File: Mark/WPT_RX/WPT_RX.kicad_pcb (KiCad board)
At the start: 2 copper layers, 53 parts, among them J1 Conn_01x01, J2 Conn_01x01, J3 SMA, J4 SMA, J5 SMA, J6 Conn_01x01, J7 Conn_01x01, J8 From PI Board, Q1 NMOS, U1 LMC6032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

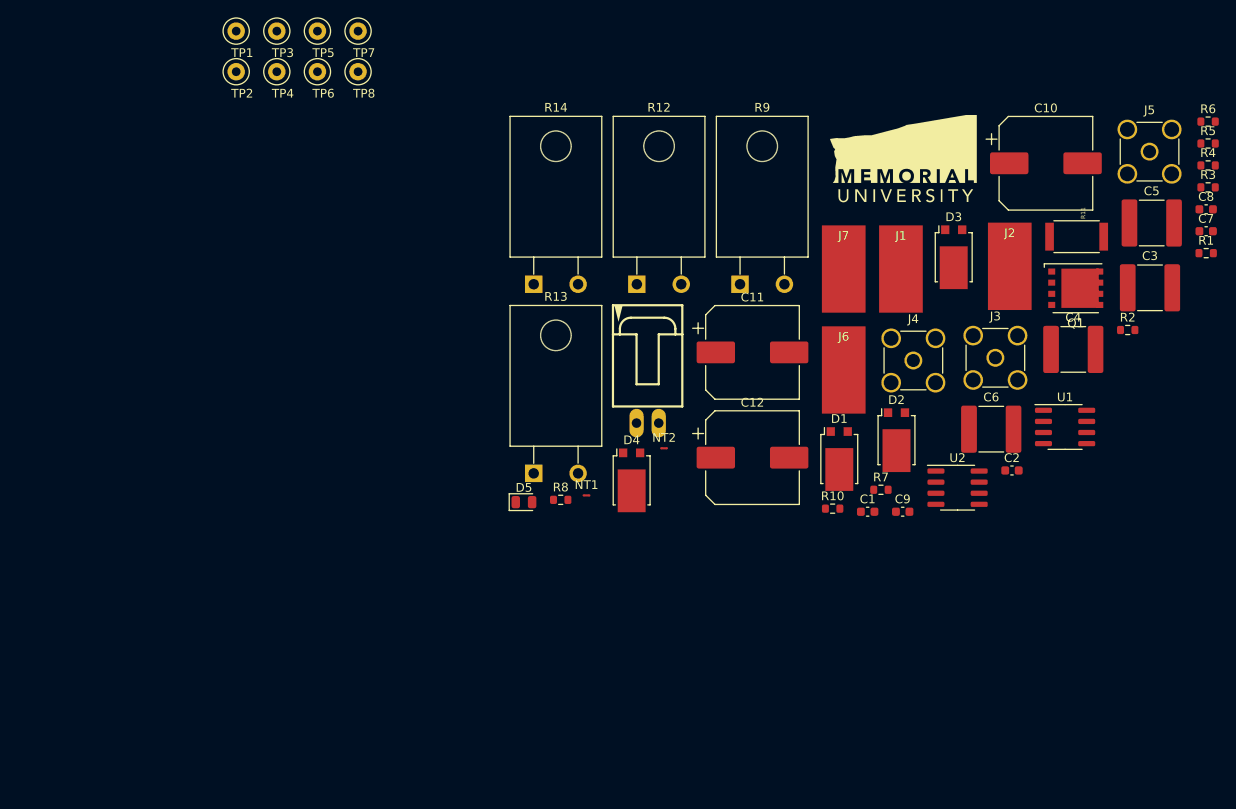
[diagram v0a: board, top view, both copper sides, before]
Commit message: RX Layout
- Completed layout
- Also cleaned up some silkscreen since I was in the zone.
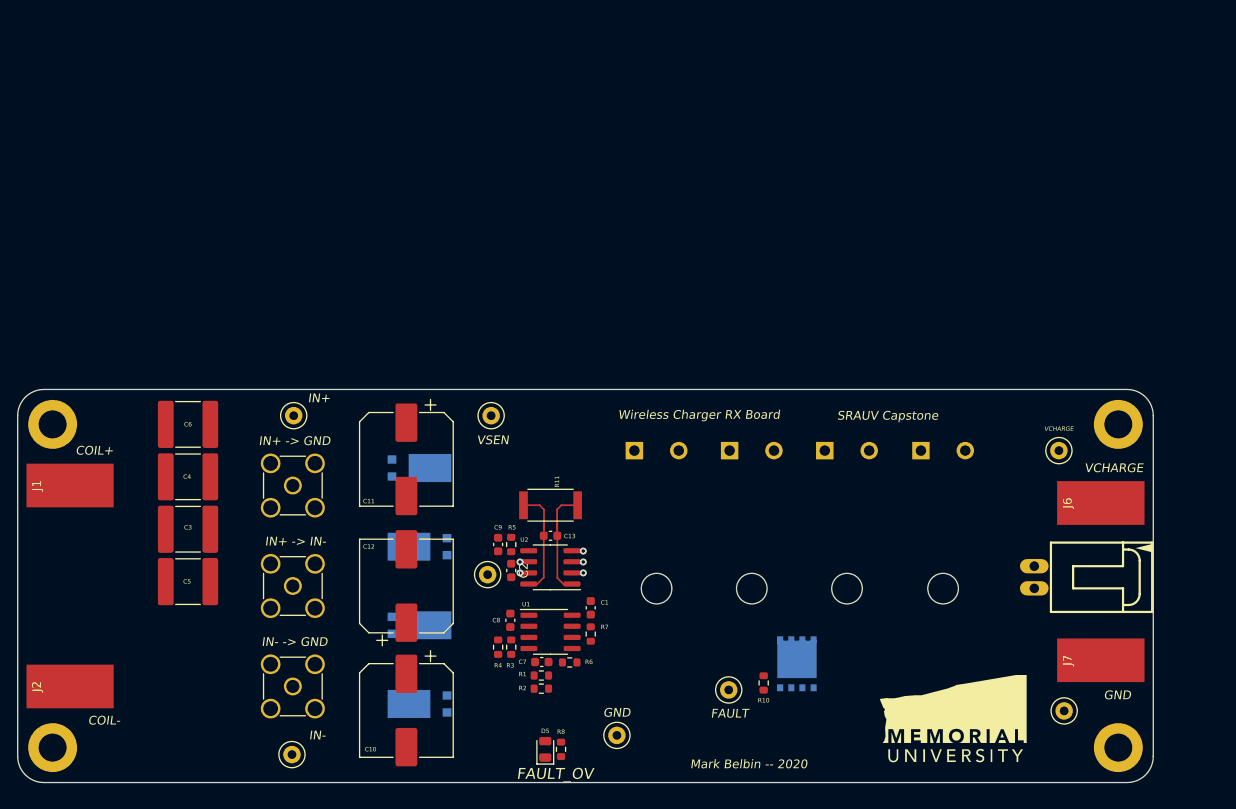
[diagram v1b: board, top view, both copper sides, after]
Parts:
- added C13: 0.1u, Capacitor_SMD:C_0603_1608Metric, F.Cu at (161.0, 116.8)
- added H1: M3, MountingHole:MountingHole_3.2mm_M3_DIN965_Pad, F.Cu at (226.0, 104.0)
- added H2: M3, MountingHole:MountingHole_3.2mm_M3_DIN965_Pad, F.Cu at (226.0, 141.0)
- added H3: M3, MountingHole:MountingHole_3.2mm_M3_DIN965_Pad, F.Cu at (104.0, 104.0)
- added H4: M3, MountingHole:MountingHole_3.2mm_M3_DIN965_Pad, F.Cu at (104.0, 141.0)
- D1, D2, D3, D4: footprint Package_TO_SOT_SMD:TO-277B -> WPT_RX:TO-277B; moved to B.Cu
- Q1, R12, R13, R14, R9: moved to B.Cu
- moved J2 117.8 mm to (106.0, 134.0), turned to 90 degrees
- moved C5 117.7 mm to (119.5, 122.0), turned to 180 degrees
- moved J5 115.6 mm to (131.5, 134.0)
- moved C3 113.5 mm to (119.5, 116.0), turned to 180 degrees
- moved TP7 112.2 mm to (219.8, 136.8)
- moved C4 102.4 mm to (119.5, 110.0), turned to 180 degrees
- moved J1 98.3 mm to (106.0, 111.0), turned to 90 degrees
- moved R4 98.2 mm to (155.0, 129.5), turned to 270 degrees
- moved C10 96.4 mm to (144.5, 136.8), turned to 270 degrees
- moved R6 95.8 mm to (163.2, 131.2), turned to 180 degrees
- moved R3 95.6 mm to (156.5, 129.5), turned to 90 degrees
- moved TP6 95.3 mm to (219.2, 107.0)
- moved C8 92.5 mm to (156.4, 126.4), turned to 90 degrees
- moved R5 92.0 mm to (156.5, 117.8), turned to 90 degrees
- moved C6 92.0 mm to (119.5, 104.0), turned to 180 degrees
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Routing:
- net /ISEN+: track 0.00 -> 7.57 mm
- net /ISEN-: track 0.00 -> 7.55 mm
- net GND: track 0.00 -> 4.92 mm, vias 0 -> 4
- net /VSEN: track 0.00 -> 4.16 mm
- net +BATT: track 0.00 -> 4.16 mm
- net +5V: track 0.00 -> 1.01 mm, vias 0 -> 1
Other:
- board outline added: 130 x 45 mm
- board text added: "COIL+"
- board text added: "COIL-"
- board text added: "FAULT"
- board text added: "FAULT_OV"
- board text added: "GND"
- board text added: "IN+"
- board text added: "IN+ -> GND"
- board text added: "IN+ -> IN-"
- board text added: "IN-"
- board text added: "IN- -> GND"
- board text added: "Mark Belbin -- 2020"
- board text added: "SRAUV Capstone"
- board text added: "VCHARGE"
- board text added: "VSEN"
- board text added: "Wireless Charger RX Board"

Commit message: More Layout
- Reduced board length, should reduce board cost.
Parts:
- R12, R13, R14, R9: footprint Package_TO_SOT_THT:TO-220F-2_Horizontal_TabDown -> WPT_RX:TO-220F-2_Horizontal_TabDown
- moved U3 29.4 mm to (169.0, 137.0)
- moved TP5 27.5 mm to (154.4, 139.6)
- moved TP7 27.3 mm to (192.5, 138.0)
- moved R14 27.3 mm to (170.6, 123.4)
- moved TP6 26.7 mm to (192.5, 108.0)
- moved J8 24.0 mm to (200.0, 121.5)
- moved H1 23.5 mm to (202.5, 104.0)
- moved H2 23.0 mm to (203.0, 141.5)
- moved J6 23.0 mm to (201.0, 113.0)
- moved J7 23.0 mm to (201.0, 131.0)
- moved R9 21.7 mm to (186.6, 120.8), turned to 180 degrees
- moved R13 16.4 mm to (181.5, 123.4)
- moved R12 14.7 mm to (175.7, 120.8), turned to 180 degrees
- moved R10 5.25 mm to (190.6, 134.3), turned to 270 degrees
- moved TP8 4.62 mm to (165.0, 136.7)
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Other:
- board size 130 x 45 mm -> 105 x 45 mm

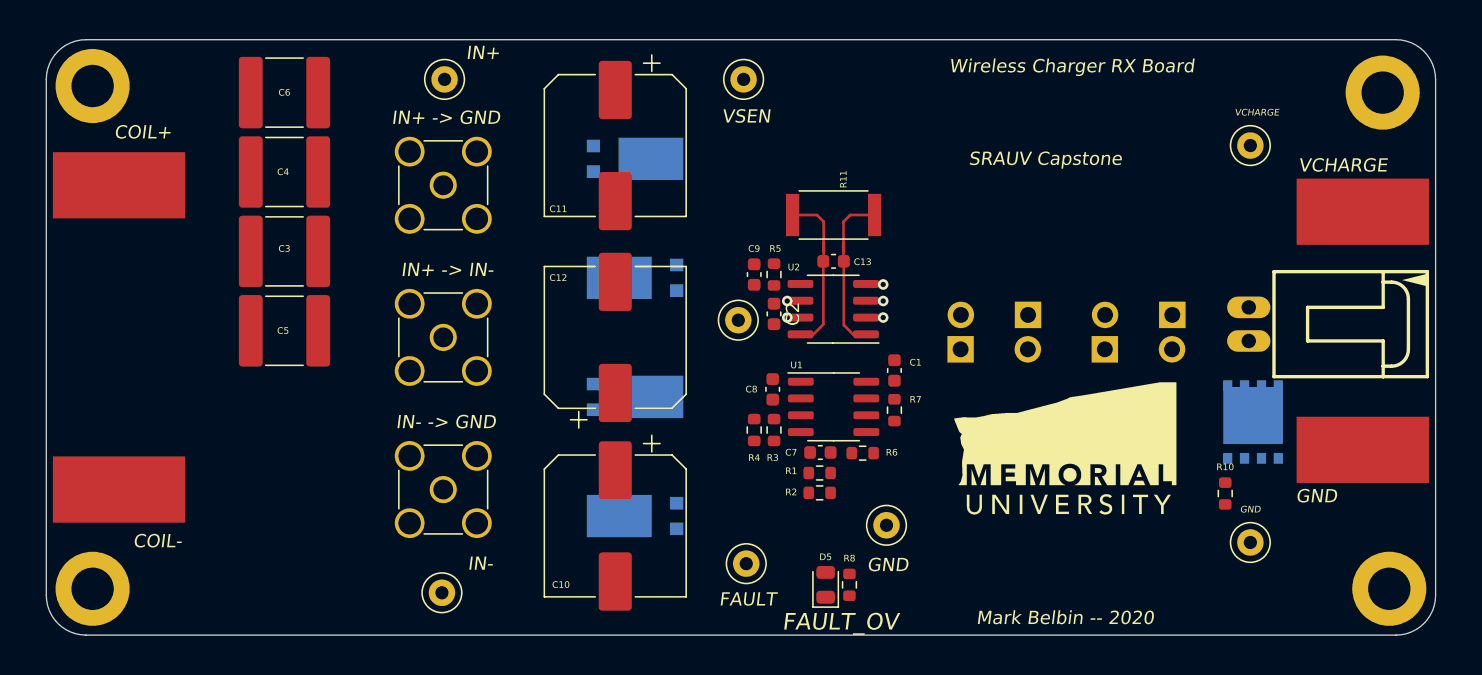
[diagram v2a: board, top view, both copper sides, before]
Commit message: Finished RX Board
- Layout and routing complete.
- Silk looks good.
- All 3D models are in there.
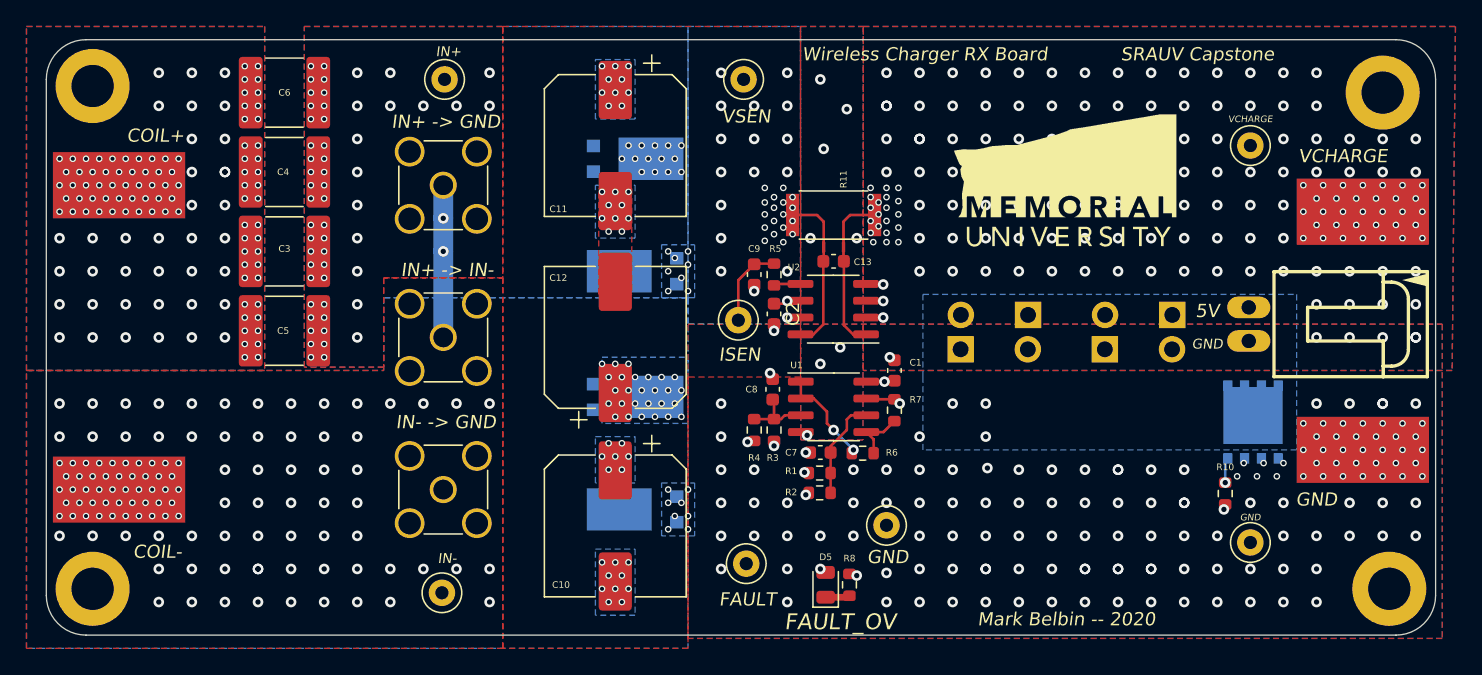
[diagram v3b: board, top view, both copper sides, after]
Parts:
- moved U3 20.2 mm to (169.0, 116.8)
- moved D4 18.5 mm to (146.0, 117.5)
- moved D2 17.5 mm to (146.0, 135.5)
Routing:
- net /FAULT_OVP: track 0.00 -> 53.9 mm, vias 0 -> 5
- net Net-(C3-Pad1): track 0.00 -> 11.5 mm, vias 0 -> 57
- net /VSEN: track 4.16 -> 13.0 mm, vias 0 -> 92
- net Net-(R6-Pad2): track 0.00 -> 7.67 mm, vias 0 -> 2
- net /VREF: track 0.00 -> 7.66 mm
- net /ISEN: track 0.00 -> 6.24 mm
- net Net-(C8-Pad1): track 0.00 -> 5.16 mm
- net GND: track 4.92 -> 9.61 mm, vias 4 -> 194
- net +5V: track 1.01 -> 5.60 mm, vias 1 -> 3
- net Net-(R6-Pad1): track 0.00 -> 4.29 mm
- net Net-(R5-Pad1): track 0.00 -> 2.05 mm
- net Net-(D5-Pad1): track 0.00 -> 1.85 mm
- net Net-(D1-Pad2): vias 0 -> 113
- net Net-(C3-Pad2): vias 0 -> 125
- net +BATT: vias 0 -> 165
- added copper zone on In2.Cu, net +5V
- added copper zone on B.Cu, net +BATT
- added copper zone on F.Cu, net +BATT
- added copper zone on B.Cu, net /VSEN
- added copper zone on F.Cu, net /VSEN
- added copper zone on In2.Cu, net /VSEN
- added copper zone on B.Cu, net GND
- added copper zone on F.Cu, net GND
- added copper zone on In1.Cu, net GND
- added copper zone on B.Cu, net Net-(C3-Pad1)
- added copper zone on F.Cu, net Net-(C3-Pad1)
- added copper zone on In2.Cu, net Net-(C3-Pad1)
- added copper zone on B.Cu, net Net-(C3-Pad2)
- added copper zone on F.Cu, net Net-(C3-Pad2)
- added copper zone on In2.Cu, net Net-(C3-Pad2)
- added copper zone on B.Cu, net Net-(D1-Pad2)
- added copper zone on F.Cu, net Net-(D1-Pad2)
- added copper zone on In2.Cu, net Net-(D1-Pad2)
- added copper zone on B.Cu, net Net-(Q1-Pad3)
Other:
- copper layers 2 -> 4
- rule via_min_size: 0.4 -> 0.3
- board text added: "5V"
- board text added: "ISEN"

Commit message: Gerbers
- Generated gerbers
- Changed TX board size to 45x100mm to match RX board.
- Ordered PCBs like the impaitent bastard I am
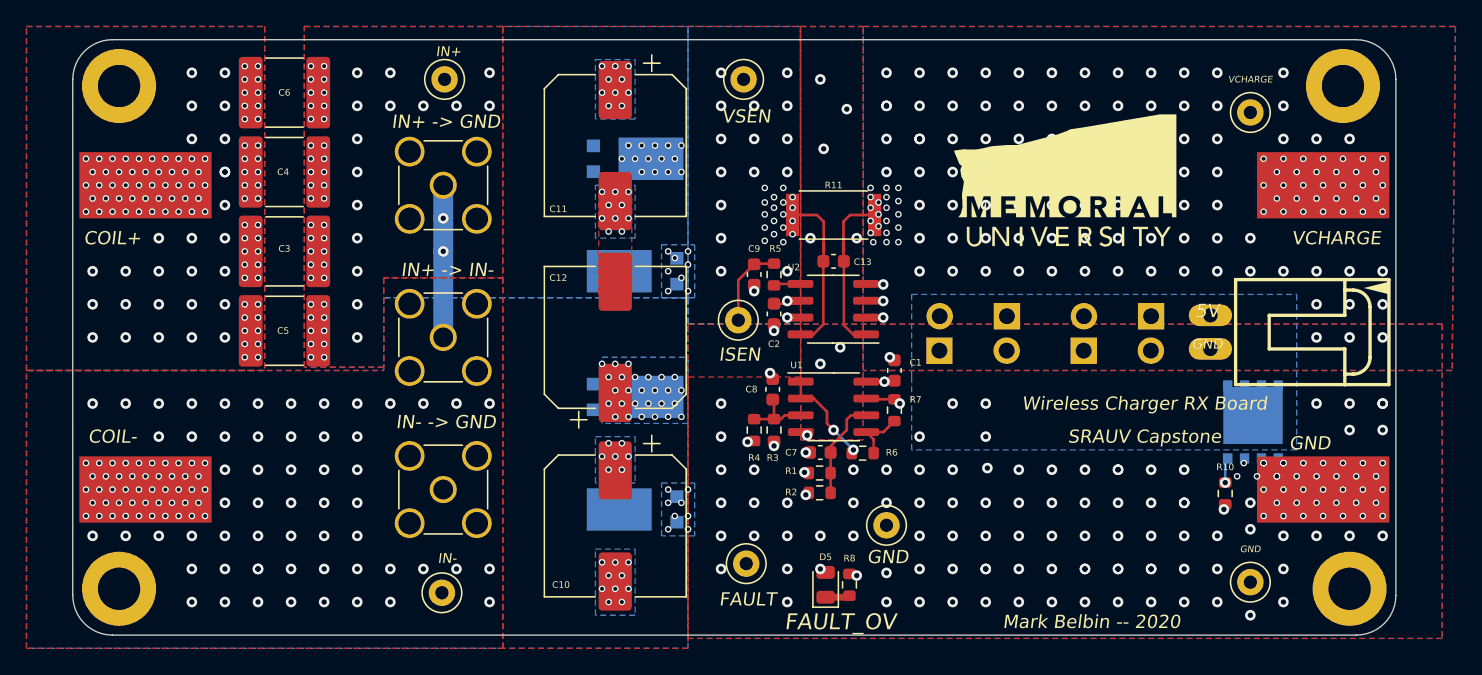
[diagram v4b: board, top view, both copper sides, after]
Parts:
- moved J7 4.24 mm to (198.0, 134.0)
- moved J6 3.61 mm to (198.0, 111.0)
- moved H1 3.04 mm to (199.5, 103.5)
- moved H2 3.00 mm to (200.0, 141.5)
- moved TP7 3.00 mm to (192.5, 141.0)
- moved J8 2.96 mm to (197.1, 122.1)
- moved TP6 2.50 mm to (192.5, 105.5)
- moved H3 2.00 mm to (107.0, 103.5)
- moved H4 2.00 mm to (107.0, 141.5)
- moved J1 2.00 mm to (109.0, 111.0)
- moved J2 2.00 mm to (109.0, 134.0)
- moved R12 1.60 mm to (174.1, 120.9)
- moved R9 1.60 mm to (185.0, 120.9)
- moved R13 1.60 mm to (179.9, 123.5)
- moved R14 1.60 mm to (169.0, 123.5)
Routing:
- net Net-(D1-Pad2): vias 113 -> 106
- net Net-(C3-Pad2): vias 125 -> 115
- net GND: vias 194 -> 188
- net +BATT: vias 165 -> 146
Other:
- board size 105 x 45 mm -> 100 x 45 mm
